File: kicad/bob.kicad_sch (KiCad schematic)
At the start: 45 parts, among them J1 GPIO (Optional), J2 Mini USB Female, J3 Battery Connector, J4 GPIO (Optional), SW1 Screw Switch, U1 RP2040, U2 W25Q64JVSS, U3 NCP1117-3.3_SOT223, U4 MPU-6050, Y1 12MHz

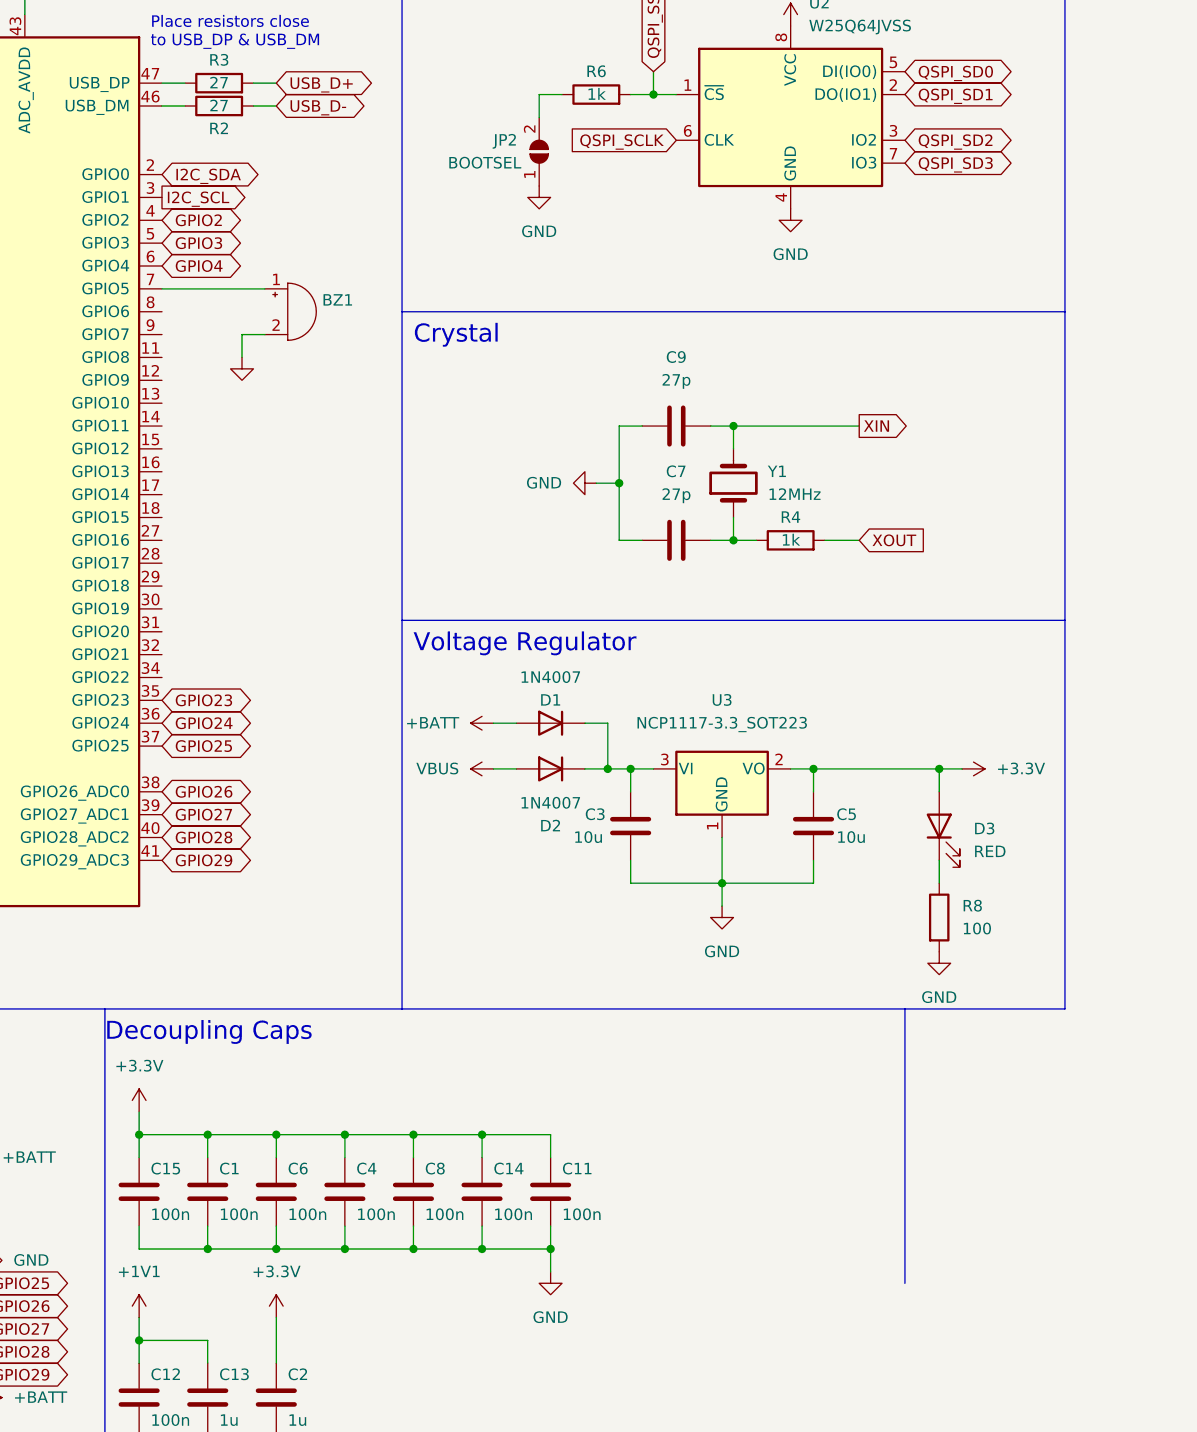
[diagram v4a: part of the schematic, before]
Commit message: Moved I2C to bottom of RP2040
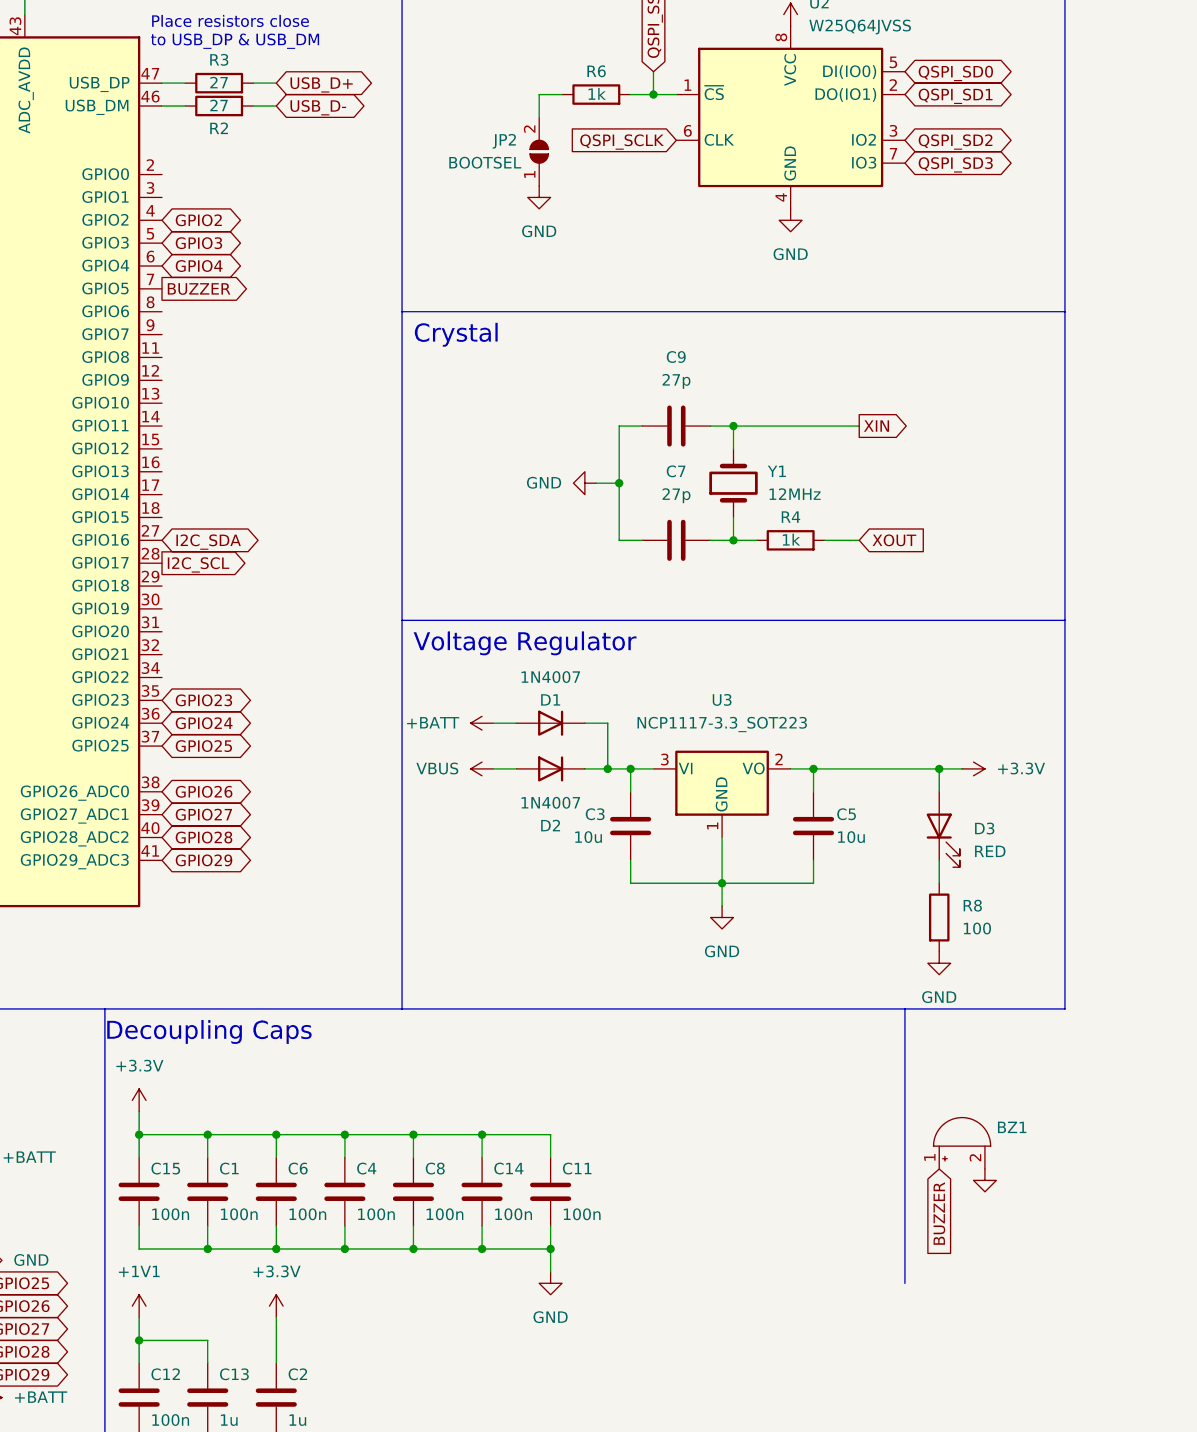
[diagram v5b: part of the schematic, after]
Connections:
- net I2C_SCL: now also U1.28 (GPIO17); no longer U1.3 (GPIO1)
- net I2C_SDA: now also U1.27 (GPIO16); no longer U1.2 (GPIO0)
- net BUZZER: now reaches BZ1.1 (-), U1.7 (GPIO5)
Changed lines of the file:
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@@
-    (stroke (width 0) (type default) (color 0 0 0 0))
-  )
-  (wire (pts (xy 104.14 60.96) (xy 104.14 63.5))
     (stroke (width 0) (type default) (color 0 0 0 0))
   )
@@
     (stroke (width 0) (type default) (color 0 0 0 0))
   )
-  (wire (pts (xy 106.68 60.96) (xy 104.14 60.96))
-    (stroke (width 0) (type default) (color 0 0 0 0))
-  )
   (wire (pts (xy 130.81 149.86) (xy 130.81 152.4))
     (stroke (width 0) (type default) (color 0 0 0 0))
@@
   )
   (polyline (pts (xy 195.58 135.89) (xy 195.58 92.71))
-    (stroke (width 0) (type default) (color 0 0 0 0))
-  )
-  (wire (pts (xy 95.25 55.88) (xy 106.68 55.88))
     (stroke (width 0) (type default) (color 0 0 0 0))
   )
@@
     )
   )
+  (global_label "BUZZER" (shape output) (at 95.25 55.88 0) (fields_autoplaced)
+    (effects (font (size 1.27 1.27)) (justify left))
+    (property "Intersheet References" "${INTERSHEET_REFS}" (id 0) (at 105.1017 55.8006 0)
+      (effects (font (size 1.27 1.27)) (justify left) hide)
+    )
+  )
   (global_label "QSPI_SD3" (shape bidirectional) (at 31.75 55.88 180) (fields_autoplaced)
     (effects (font (size 1.27 1.27)) (justify right))
@@
     )
   )
-  (global_label "I2C_SDA" (shape bidirectional) (at 95.25 43.18 0) (fields_autoplaced)
-    (effects (font (size 1.27 1.27)) (justify left))
-    (property "Intersheet References" "${INTERSHEET_REFS}" (id 0) (at 105.2831 43.1006 0)
-      (effects (font (size 1.27 1.27)) (justify left) hide)
-    )
-  )
   (global_label "QSPI_SD2" (shape bidirectional) (at 177.8 39.37 0) (fields_autoplaced)
     (effects (font (size 1.27 1.27)) (justify left))
@@
     )
   )
+  (global_label "I2C_SDA" (shape bidirectional) (at 95.25 83.82 0) (fields_autoplaced)
+    (effects (font (size 1.27 1.27)) (justify left))
+    (property "Intersheet References" "${INTERSHEET_REFS}" (id 0) (at 105.2831 83.7406 0)
+      (effects (font (size 1.27 1.27)) (justify left) hide)
+    )
+  )
   (global_label "GPIO2" (shape bidirectional) (at 95.25 48.26 0) (fields_autoplaced)
     (effects (font (size 1.27 1.27)) (justify left))
@@
     (effects (font (size 1.27 1.27)) (justify left))
     (property "Intersheet References" "${INTERSHEET_REFS}" (id 0) (at 41.7831 162.4806 0)
+      (effects (font (size 1.27 1.27)) (justify left) hide)
+    )
+  )
+  (global_label "I2C_SCL" (shape output) (at 95.25 86.36 0) (fields_autoplaced)
+    (effects (font (size 1.27 1.27)) (justify left))
+    (property "Intersheet References" "${INTERSHEET_REFS}" (id 0) (at 105.2226 86.2806 0)
       (effects (font (size 1.27 1.27)) (justify left) hide)
     )
@@
     )
   )
+  (global_label "BUZZER" (shape input) (at 181.61 153.67 270) (fields_autoplaced)
+    (effects (font (size 1.27 1.27)) (justify right))
+    (property "Intersheet References" "${INTERSHEET_REFS}" (id 0) (at 181.5306 163.5217 90)
+      (effects (font (size 1.27 1.27)) (justify right) hide)
+    )
+  )
   (global_label "QSPI_SD0" (shape bidirectional) (at 31.75 48.26 180) (fields_autoplaced)
     (effects (font (size 1.27 1.27)) (justify right))
@@
     )
   )
-  (global_label "I2C_SCL" (shape output) (at 95.25 45.72 0) (fields_autoplaced)
-    (effects (font (size 1.27 1.27)) (justify left))
-    (property "Intersheet References" "${INTERSHEET_REFS}" (id 0) (at 105.2226 45.6406 0)
-      (effects (font (size 1.27 1.27)) (justify left) hide)
-    )
-  )
   (global_label "GPIO25" (shape bidirectional) (at 95.25 106.68 0) (fields_autoplaced)
     (effects (font (size 1.27 1.27)) (justify left))
@@
     (pin "2")
   )
-  (symbol (lib_id "Device:Buzzer") (at 109.22 58.42 0) (unit 1)
-    (in_bom yes) (on_board yes) (fields_autoplaced)
-    (property "Reference" "BZ1" (id 0) (at 113.03 57.1499 0)
-      (effects (font (size 1.27 1.27)) (justify left))
-    )
-    (property "Value" "" (id 1) (at 113.03 59.6899 0)
-      (effects (font (size 1.27 1.27)) (justify left))
-    )
-    (property "Footprint" "" (id 2) (at 108.585 55.88 90)
-      (effects (font (size 1.27 1.27)) hide)
-    )
-    (property "Datasheet" "~" (id 3) (at 108.585 55.88 90)
-      (effects (font (size 1.27 1.27)) hide)
-    )
-    (pin "1")
-    (pin "2")
-  )
   (symbol (lib_id "power:+1V1") (at 46.99 20.32 0) (unit 1)
     (in_bom yes) (on_board yes) (fields_autoplaced)
@@
     (pin "1")
     (pin "2")
-  )
-  (symbol (lib_id "power:GND") (at 104.14 63.5 0) (unit 1)
-    (in_bom yes) (on_board yes) (fields_autoplaced)
-    (property "Reference" "#PWR?" (id 0) (at 104.14 69.85 0)
-      (effects (font (size 1.27 1.27)) hide)
-    )
-    (property "Value" "" (id 1) (at 104.14 68.58 0))
-    (property "Footprint" "" (id 2) (at 104.14 63.5 0)
-      (effects (font (size 1.27 1.27)) hide)
-    )
-    (property "Datasheet" "" (id 3) (at 104.14 63.5 0)
-      (effects (font (size 1.27 1.27)) hide)
-    )
-    (pin "1")
   )
   (symbol (lib_id "Device:R") (at 16.51 90.17 0) (unit 1)
@@
     (pin "8")
   )
+  (symbol (lib_id "power:GND") (at 186.69 153.67 0) (unit 1)
+    (in_bom yes) (on_board yes) (fields_autoplaced)
+    (property "Reference" "#PWR?" (id 0) (at 186.69 160.02 0)
+      (effects (font (size 1.27 1.27)) hide)
+    )
+    (property "Value" "" (id 1) (at 186.69 158.75 0))
+    (property "Footprint" "" (id 2) (at 186.69 153.67 0)
+      (effects (font (size 1.27 1.27)) hide)
+    )
+    (property "Datasheet" "" (id 3) (at 186.69 153.67 0)
+      (effects (font (size 1.27 1.27)) hide)
+    )
+    (pin "1")
+  )
   (symbol (lib_id "Device:C") (at 147.32 115.57 0) (mirror y) (unit 1)
     (in_bom yes) (on_board yes)
@@
     )
     (property "Datasheet" "~" (id 3) (at 152.4 71.12 0)
+      (effects (font (size 1.27 1.27)) hide)
+    )
+    (pin "1")
+    (pin "2")
+  )
+  (symbol (lib_id "Device:Buzzer") (at 184.15 151.13 90) (unit 1)
+    (in_bom yes) (on_board yes) (fields_autoplaced)
+    (property "Reference" "BZ1" (id 0) (at 187.96 149.0979 90)
+      (effects (font (size 1.27 1.27)) (justify right))
+    )
+    (property "Value" "" (id 1) (at 187.96 151.6379 90)
+      (effects (font (size 1.27 1.27)) (justify right))
+    )
+    (property "Footprint" "" (id 2) (at 181.61 151.765 90)
+      (effects (font (size 1.27 1.27)) hide)
+    )
+    (property "Datasheet" "~" (id 3) (at 181.61 151.765 90)
       (effects (font (size 1.27 1.27)) hide)
     )
@@
       (reference "#PWR0140") (unit 1) (value "GND") (footprint "")
     )
-    (path "/16cdadb5-6329-4729-9c41-af8600d7857b"
+    (path "/46227f9b-4f9d-4b2b-b3bd-94b2e925422e"
       (reference "#PWR?") (unit 1) (value "GND") (footprint "")
     )
@@
       (reference "#PWR?") (unit 1) (value "GND") (footprint "")
     )
-    (path "/0c0afd09-1d3f-47c4-bdfb-8409bb16aa71"
-      (reference "BZ1") (unit 1) (value "Buzzer") (footprint "Buzzer_Beeper:Buzzer_12x9.5RM7.6")
+    (path "/e65ef186-5520-4142-8b10-d2898e4cdc2f"
+      (reference "BZ1") (unit 1) (value "Buzzer") (footprint "")
     )
     (path "/00b942de-1e62-476c-a78f-85d1dc0d5dee"

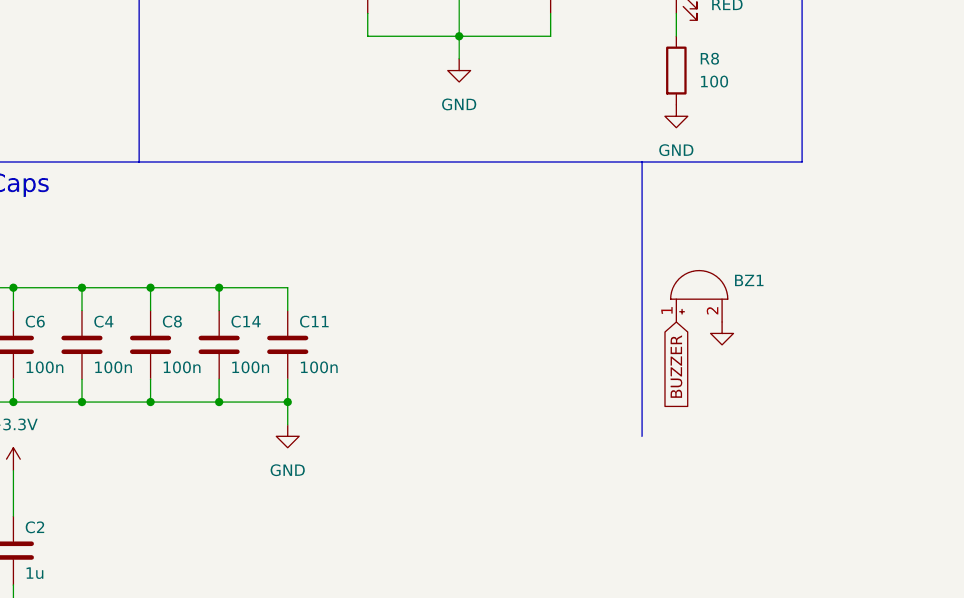
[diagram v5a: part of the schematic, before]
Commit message: Changed 0402s to 0603s
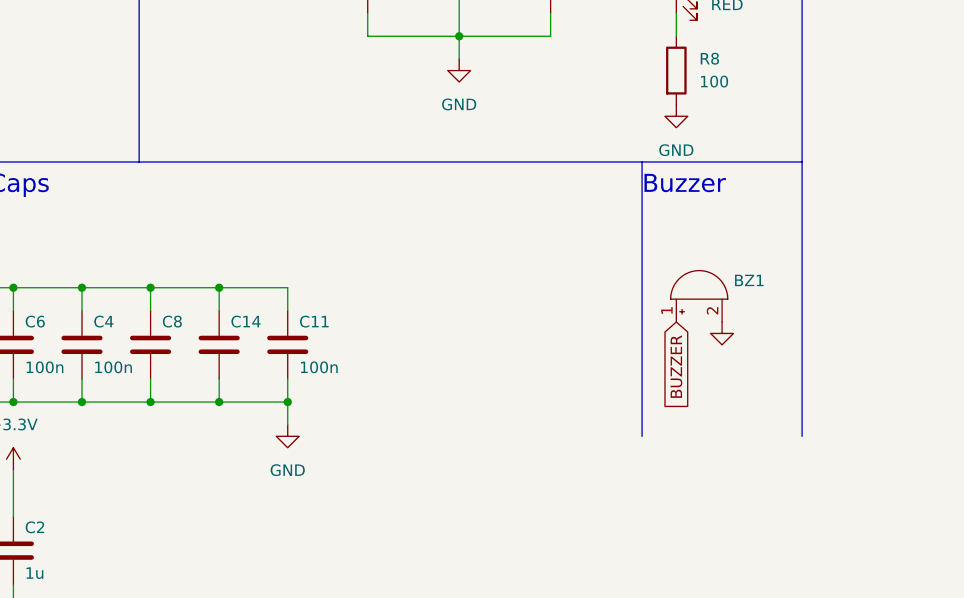
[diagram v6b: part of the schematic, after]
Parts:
- C14, C8: value 100n -> (none); footprint Capacitor_SMD:C_0402_1005Metric -> (none)
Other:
- note added: "Buzzer"
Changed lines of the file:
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@@
+    (stroke (width 0) (type default) (color 0 0 0 0))
+  )
+  (polyline (pts (xy 195.58 135.89) (xy 195.58 166.37))
     (stroke (width 0) (type default) (color 0 0 0 0))
   )
@@
   )
   (text "I2C Bus" (at 196.85 16.51 0)
+    (effects (font (size 2 2)) (justify left bottom))
+  )
+  (text "Buzzer" (at 177.8 139.7 0)
     (effects (font (size 2 2)) (justify left bottom))
   )
@@
       (effects (font (size 1.27 1.27)) (justify left))
     )
-    (property "Value" "100n" (id 1) (at 124.46 158.75 0)
-      (effects (font (size 1.27 1.27)) (justify left))
-    )
-    (property "Footprint" "Capacitor_SMD:C_0402_1005Metric" (id 2) (at 124.1552 160.02 0)
+    (property "Value" "" (id 1) (at 124.46 158.75 0)
+      (effects (font (size 1.27 1.27)) (justify left))
+    )
+    (property "Footprint" "" (id 2) (at 124.1552 160.02 0)
       (effects (font (size 1.27 1.27)) hide)
     )
@@
       (effects (font (size 1.27 1.27)) (justify left))
     )
-    (property "Value" "100n" (id 1) (at 132.08 158.75 0)
-      (effects (font (size 1.27 1.27)) (justify left))
-    )
-    (property "Footprint" "Capacitor_SMD:C_0402_1005Metric" (id 2) (at 131.7752 160.02 0)
+    (property "Value" "" (id 1) (at 132.08 158.75 0)
+      (effects (font (size 1.27 1.27)) (justify left))
+    )
+    (property "Footprint" "" (id 2) (at 131.7752 160.02 0)
       (effects (font (size 1.27 1.27)) hide)
     )
@@
     )
     (path "/ba9eb375-d457-4f26-a90e-bfaa41cc45cb"
-      (reference "C14") (unit 1) (value "100n") (footprint "Capacitor_SMD:C_0402_1005Metric")
+      (reference "C14") (unit 1) (value "100n") (footprint "Capacitor_SMD:C_0603_1608Metric")
     )
     (path "/2f172b15-c4a0-413b-9387-1422f3435e76"
